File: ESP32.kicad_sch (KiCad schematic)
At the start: 20 parts, among them Q1 SS8050-G, Q2 SS8050-G, U2 ESP32-WROOM-32E-H4, U3 DF52-5S-0.8H(21), U5 CP2102N-A02-GQFN24R

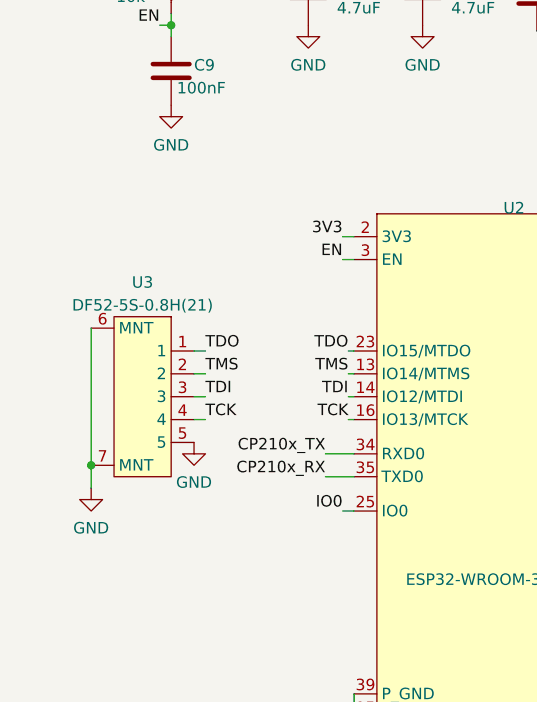
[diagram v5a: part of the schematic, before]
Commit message: exposed boot and IO0 on jtag connector for esp32
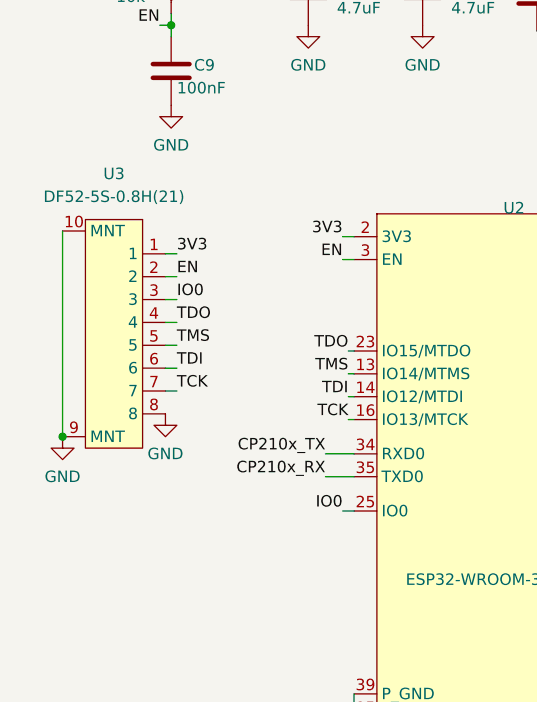
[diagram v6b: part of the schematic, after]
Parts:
- U3: footprint robot-cortex:DF52-5S-0.8H(21) -> robot-cortex:DF52-8S-0.8H(21); symbol robot-cortex:DF52-5S-0.8H(21) -> robot-cortex:DF52-8S-0.8H(21)
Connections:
- net 3V3: now also U3.1
- net EN: now also U3.2
- net GND: now also U3.10 (MNT), U3.8, U3.9 (MNT); no longer U3.5, U3.6 (MNT), U3.7 (MNT)
- net IO0: now also U3.3
- net TCK: now also U3.7; no longer U3.4
- net TDI: now also U3.6; no longer U3.3
- net TDO: now also U3.4; no longer U3.1
- net TMS: now also U3.5; no longer U3.2
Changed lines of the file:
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@@
   (junction (at 29.21 40.005) (diameter 0) (color 0 0 0 0)
   )
+  (junction (at 17.145 85.725) (diameter 0) (color 0 0 0 0)
+  )
   (junction (at 49.53 119.38) (diameter 0) (color 0 0 0 0)
   )
@@
   )
   (junction (at 76.2 33.02) (diameter 0) (color 0 0 0 0)
-  )
-  (junction (at 20.32 88.9) (diameter 0) (color 0 0 0 0)
   )
   (junction (at 49.53 116.84) (diameter 0) (color 0 0 0 0)
@@
   (no_connect (at 211.455 128.905))
   (no_connect (at 257.175 139.065))
-  (wire (pts (xy 33.02 81.28) (xy 31.75 81.28))
-    (stroke (width 0) (type default))
-  )
-  (wire (pts (xy 33.02 78.74) (xy 31.75 78.74))
+  (wire (pts (xy 29.845 78.105) (xy 28.575 78.105))
+    (stroke (width 0) (type default))
+  )
+  (wire (pts (xy 29.845 75.565) (xy 28.575 75.565))
     (stroke (width 0) (type default))
   )
@@
     (stroke (width 0) (type default))
   )
-  (wire (pts (xy 33.02 76.2) (xy 31.75 76.2))
+  (wire (pts (xy 29.845 73.025) (xy 28.575 73.025))
     (stroke (width 0) (type default))
   )
@@
     (stroke (width 0) (type default))
   )
+  (wire (pts (xy 29.845 67.945) (xy 28.575 67.945))
+    (stroke (width 0) (type default))
+  )
   (wire (pts (xy 253.365 48.895) (xy 253.365 48.26))
     (stroke (width 0) (type default))
@@
     (stroke (width 0) (type default))
   )
+  (wire (pts (xy 29.845 65.405) (xy 28.575 65.405))
+    (stroke (width 0) (type default))
+  )
   (wire (pts (xy 264.795 116.205) (xy 257.175 116.205))
     (stroke (width 0) (type default))
@@
     (stroke (width 0) (type default))
   )
+  (wire (pts (xy 29.845 70.485) (xy 28.575 70.485))
+    (stroke (width 0) (type default))
+  )
   (wire (pts (xy 48.895 83.82) (xy 49.53 83.82))
     (stroke (width 0) (type default))
@@
     (stroke (width 0) (type default))
   )
-  (wire (pts (xy 20.32 91.44) (xy 20.32 88.9))
-    (stroke (width 0) (type default))
-  )
   (wire (pts (xy 214.63 82.55) (xy 222.25 82.55))
     (stroke (width 0) (type default))
@@
     (stroke (width 0) (type default))
   )
-  (wire (pts (xy 33.02 83.82) (xy 31.75 83.82))
+  (wire (pts (xy 29.845 80.645) (xy 28.575 80.645))
     (stroke (width 0) (type default))
   )
@@
     (stroke (width 0) (type default))
   )
-  (wire (pts (xy 20.32 88.9) (xy 20.32 73.66))
+  (wire (pts (xy 17.145 62.865) (xy 17.145 85.725))
     (stroke (width 0) (type default))
   )
@@
     (effects (font (size 1.27 1.27)) (justify right bottom))
   )
+  (label "3V3" (at 29.845 65.405 0) (fields_autoplaced)
+    (effects (font (size 1.27 1.27)) (justify left bottom))
+  )
   (label "3V3" (at 97.79 31.75 180) (fields_autoplaced)
     (effects (font (size 1.27 1.27)) (justify right bottom))
@@
     (effects (font (size 1.27 1.27)) (justify right bottom))
   )
+  (label "IO0" (at 29.845 70.485 0) (fields_autoplaced)
+    (effects (font (size 1.27 1.27)) (justify left bottom))
+  )
   (label "ESP32_MISO" (at 90.805 109.22 0) (fields_autoplaced)
     (effects (font (size 1.27 1.27)) (justify left bottom))
   )
-  (label "TDI" (at 33.02 81.28 0) (fields_autoplaced)
+  (label "TDI" (at 29.845 78.105 0) (fields_autoplaced)
     (effects (font (size 1.27 1.27)) (justify left bottom))
   )
@@
     (effects (font (size 1.27 1.27)) (justify right bottom))
   )
+  (label "EN" (at 29.845 67.945 0) (fields_autoplaced)
+    (effects (font (size 1.27 1.27)) (justify left bottom))
+  )
   (label "3V3" (at 57.15 32.385 180) (fields_autoplaced)
     (effects (font (size 1.27 1.27)) (justify right bottom))
@@
     (effects (font (size 1.27 1.27)) (justify right bottom))
   )
-  (label "TDO" (at 33.02 76.2 0) (fields_autoplaced)
+  (label "TDO" (at 29.845 73.025 0) (fields_autoplaced)
     (effects (font (size 1.27 1.27)) (justify left bottom))
   )
@@
     (effects (font (size 1.27 1.27)) (justify right bottom))
   )
-  (label "TMS" (at 33.02 78.74 0) (fields_autoplaced)
+  (label "TMS" (at 29.845 75.565 0) (fields_autoplaced)
     (effects (font (size 1.27 1.27)) (justify left bottom))
   )
@@
     (effects (font (size 1.27 1.27)) (justify left bottom))
   )
-  (label "TCK" (at 33.02 83.82 0) (fields_autoplaced)
+  (label "TCK" (at 29.845 80.645 0) (fields_autoplaced)
     (effects (font (size 1.27 1.27)) (justify left bottom))
   )
@@
     )
   )
-  (symbol (lib_id "power:GND") (at 31.75 86.36 0) (mirror y) (unit 1)
-    (in_bom yes) (on_board yes) (dnp no) (fields_autoplaced)
-    (property "Reference" "#PWR08" (at 31.75 92.71 0)
-      (effects (font (size 1.27 1.27)) hide)
-    )
-    (property "Value" "GND" (at 31.75 90.805 0)
-      (effects (font (size 1.27 1.27)))
-    )
-    (property "Footprint" "" (at 31.75 86.36 0)
-      (effects (font (size 1.27 1.27)) hide)
-    )
-    (property "Datasheet" "" (at 31.75 86.36 0)
+  (symbol (lib_id "power:GND") (at 28.575 83.185 0) (mirror y) (unit 1)
+    (in_bom yes) (on_board yes) (dnp no) (fields_autoplaced)
+    (property "Reference" "#PWR08" (at 28.575 89.535 0)
+      (effects (font (size 1.27 1.27)) hide)
+    )
+    (property "Value" "GND" (at 28.575 87.63 0)
+      (effects (font (size 1.27 1.27)))
+    )
+    (property "Footprint" "" (at 28.575 83.185 0)
+      (effects (font (size 1.27 1.27)) hide)
+    )
+    (property "Datasheet" "" (at 28.575 83.185 0)
       (effects (font (size 1.27 1.27)) hide)
     )
@@
     )
   )
-  (symbol (lib_id "robot-cortex:DF52-5S-0.8H(21)") (at 25.4 81.28 0) (mirror y) (unit 1)
-    (in_bom yes) (on_board yes) (dnp no) (fields_autoplaced)
-    (property "Reference" "U3" (at 26.035 68.58 0)
-      (effects (font (size 1.27 1.27)))
-    )
-    (property "Value" "DF52-5S-0.8H(21)" (at 26.035 71.12 0)
-      (effects (font (size 1.27 1.27)))
-    )
-    (property "Footprint" "robot-cortex:DF52-5S-0.8H(21)" (at 22.86 93.98 0)
-      (effects (font (size 1.27 1.27)) hide)
-    )
-    (property "Datasheet" "" (at 22.86 82.55 0)
-      (effects (font (size 1.27 1.27)) hide)
-    )
-    (pin "1")
+  (symbol (lib_id "robot-cortex:DF52-8S-0.8H(21)") (at 23.495 73.025 0) (mirror y) (unit 1)
+    (in_bom yes) (on_board yes) (dnp no) (fields_autoplaced)
+    (property "Reference" "U3" (at 22.86 56.515 0)
+      (effects (font (size 1.27 1.27)))
+    )
+    (property "Value" "DF52-5S-0.8H(21)" (at 22.86 59.055 0)
+      (effects (font (size 1.27 1.27)))
+    )
+    (property "Footprint" "robot-cortex:DF52-8S-0.8H(21)" (at 20.955 93.345 0)
+      (effects (font (size 1.27 1.27)) hide)
+    )
+    (property "Datasheet" "" (at 19.685 74.295 0)
+      (effects (font (size 1.27 1.27)) hide)
+    )
+    (pin "1")
+    (pin "10")
     (pin "2")
     (pin "3")
@@
     (pin "6")
     (pin "7")
+    (pin "8")
+    (pin "9")
     (instances
       (project "robot-cortex"
@@
     )
   )
-  (symbol (lib_id "power:GND") (at 20.32 91.44 0) (mirror y) (unit 1)
-    (in_bom yes) (on_board yes) (dnp no) (fields_autoplaced)
-    (property "Reference" "#PWR07" (at 20.32 97.79 0)
-      (effects (font (size 1.27 1.27)) hide)
-    )
-    (property "Value" "GND" (at 20.32 95.885 0)
-      (effects (font (size 1.27 1.27)))
-    )
-    (property "Footprint" "" (at 20.32 91.44 0)
-      (effects (font (size 1.27 1.27)) hide)
-    )
-    (property "Datasheet" "" (at 20.32 91.44 0)
-      (effects (font (size 1.27 1.27)) hide)
-    )
+  (symbol (lib_id "power:GND") (at 17.145 85.725 0) (mirror y) (unit 1)
+    (in_bom yes) (on_board yes) (dnp no) (fields_autoplaced)
+    (property "Reference" "#PWR07" (at 17.145 92.075 0)
+      (effects (font (size 1.27 1.27)) hide)
+    )
+    (property "Value" "GND" (at 17.145 90.17 0)
+      (effects (font (size 1.27 1.27)))
+    )
+    (property "Footprint" "" (at 17.145 85.725 0)
+      (effects (font (size 1.27 1.27)) hide)
+    )
+    (property "Datasheet" "" (at 17.145 85.725 0)
+      (effects (font (size 1.27 1.27)) hide)
+    )

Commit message: placement mostly done and routing in progress
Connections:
- net BOOT: now also U2.36 (IO22); no longer U2.12 (IO27)
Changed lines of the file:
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@@
-    (stroke (width 0) (type default))
-  )
-  (wire (pts (xy 85.09 88.9) (xy 97.155 88.9))
     (stroke (width 0) (type default))
   )
@@
   )
   (wire (pts (xy 210.185 144.145) (xy 211.455 144.145))
+    (stroke (width 0) (type default))
+  )
+  (wire (pts (xy 95.25 115.57) (xy 85.09 115.57))
     (stroke (width 0) (type default))
   )
@@
     (effects (font (size 1.27 1.27)) (justify right bottom))
   )
+  (hierarchical_label "BOOT" (shape input) (at 95.25 115.57 0) (fields_autoplaced)
+    (effects (font (size 1.27 1.27)) (justify left))
+  )
   (hierarchical_label "VUSB" (shape input) (at 78.74 171.45 180) (fields_autoplaced)
     (effects (font (size 1.27 1.27)) (justify right))
@@
     (effects (font (size 1.27 1.27)) (justify left))
   )
-  (hierarchical_label "BOOT" (shape input) (at 97.155 88.9 0) (fields_autoplaced)
-    (effects (font (size 1.27 1.27)) (justify left))
-  )

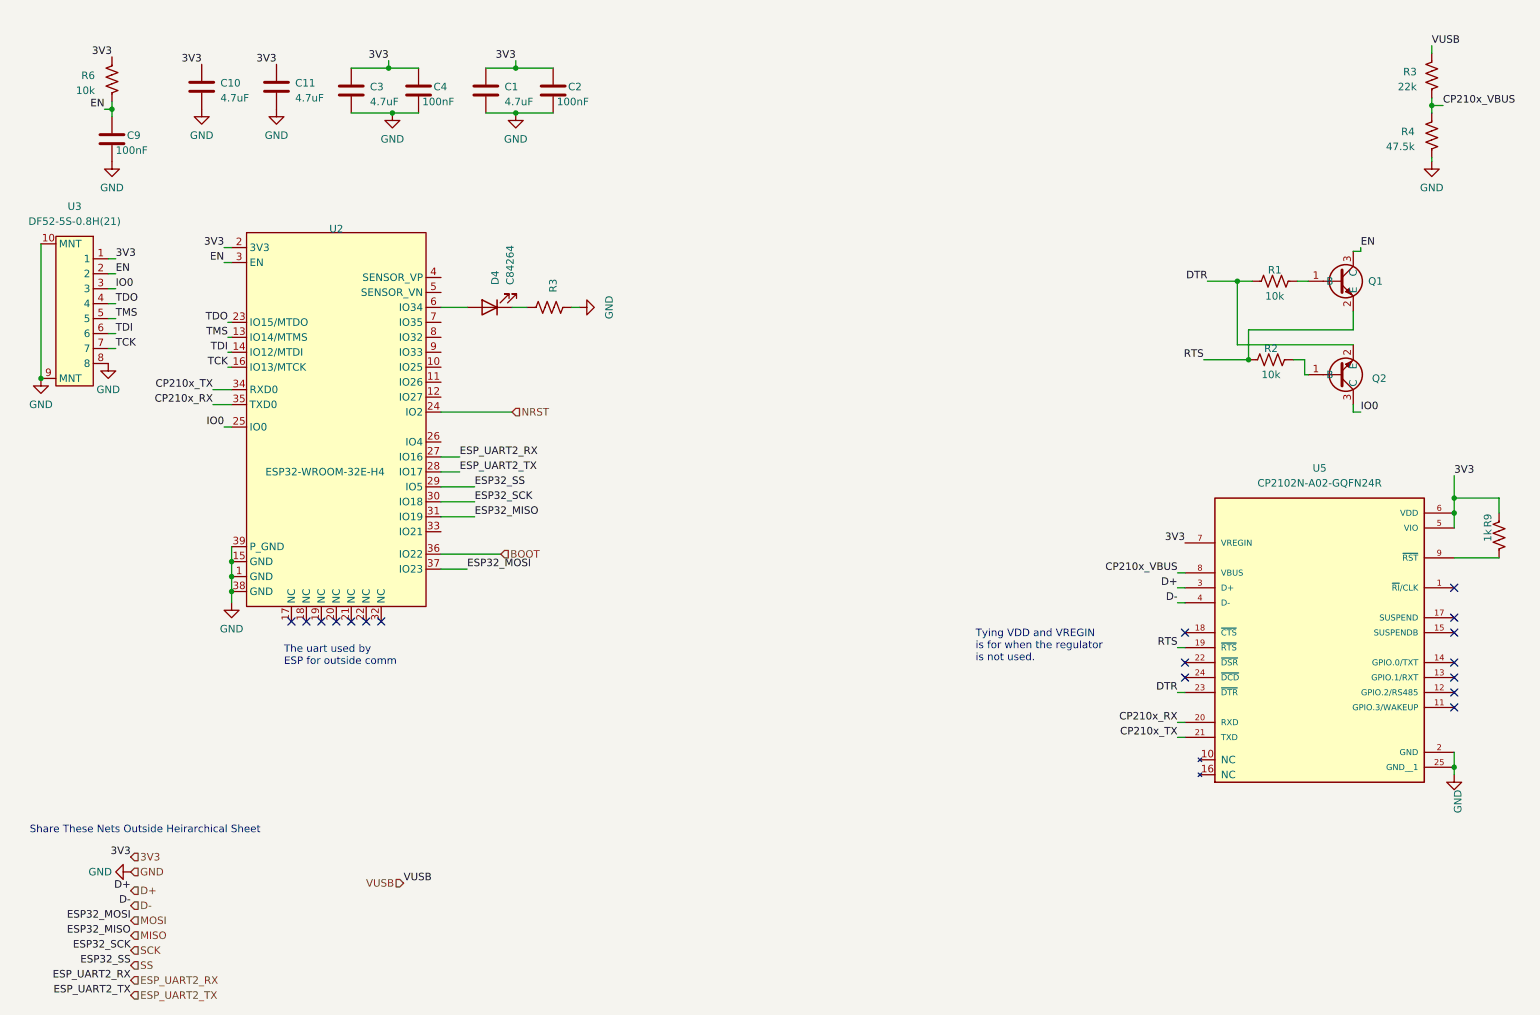
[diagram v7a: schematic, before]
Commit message: mpn correction
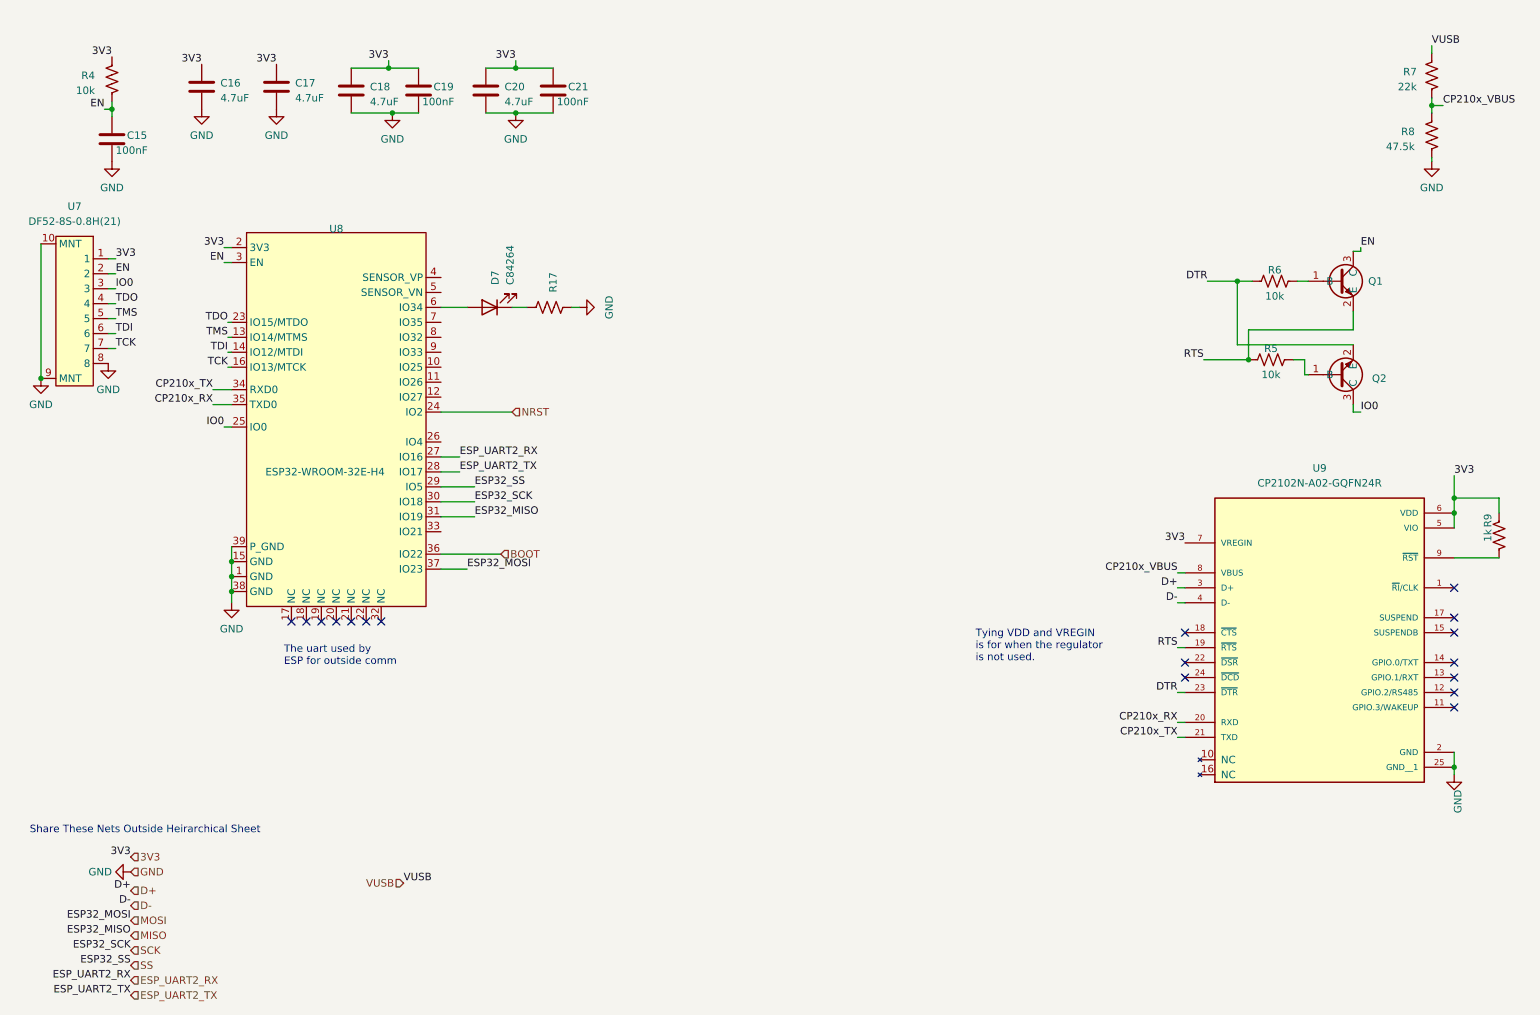
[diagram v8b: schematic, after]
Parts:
- U7: renamed from U3; value DF52-5S-0.8H(21) -> DF52-8S-0.8H(21)
- renumbered C9 to C15, C10 to C16, C11 to C17, C3 to C18, C4 to C19, C1 to C20, C2 to C21, D4 to D7, R3 to R17, R6 to R4, R2 to R5, R1 to R6, R3 to R7, R4 to R8, U2 to U8, U5 to U9
